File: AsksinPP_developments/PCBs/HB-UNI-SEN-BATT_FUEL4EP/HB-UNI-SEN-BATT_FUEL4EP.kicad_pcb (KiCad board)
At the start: 2 copper layers, 75 x 75 mm, 25 parts, among them J1 Conn_01x02, J10 charge, J2 Conn_01x02, J3 Conn_01x02, J4 Conn_01x02, J5 ISP Programmer, J6 Conn_01x04, J7 Conn_01x04, J8 Conn_01x04, J9 Conn_01x04, Q1 IRLU024N, SW1 config button

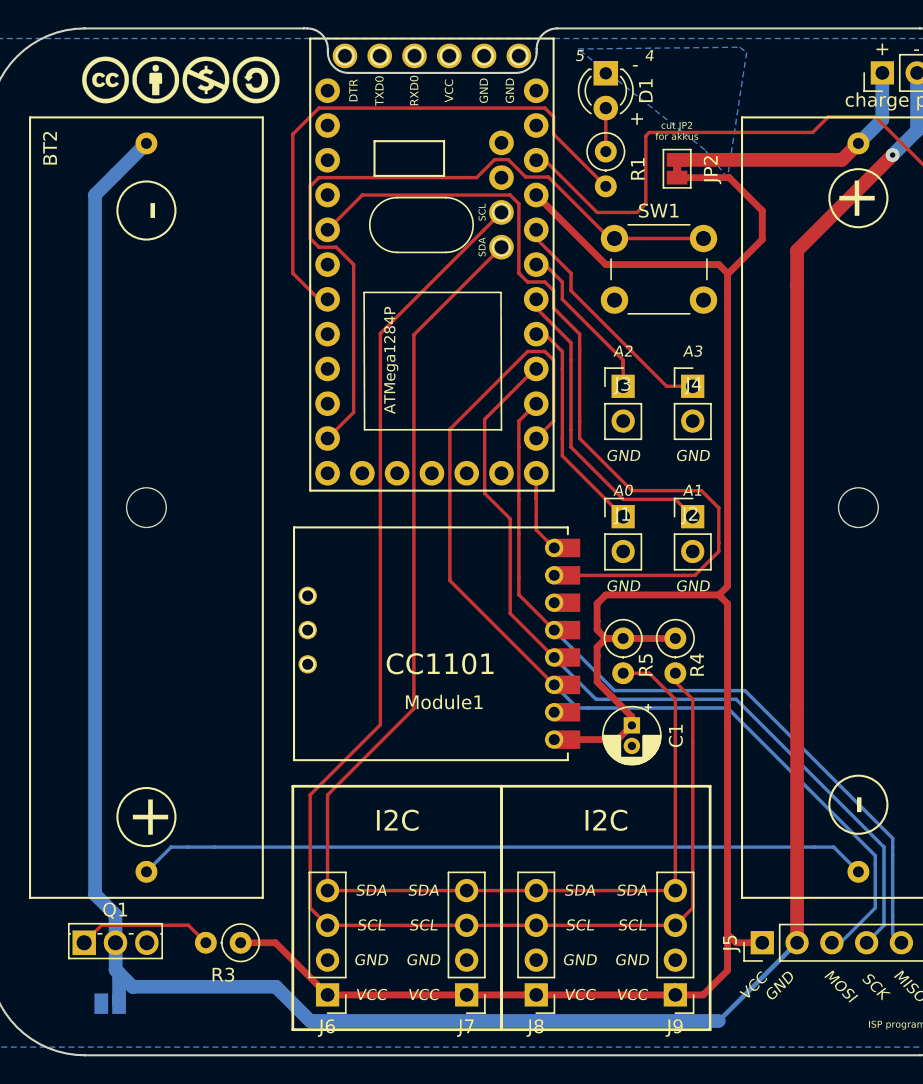
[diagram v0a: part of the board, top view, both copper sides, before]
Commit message: PCBs/HB-UNI-SEN-BATT_FUEL4EP updates, now with gerber data for JLCPCB (not yet vaalidated by prototype!)
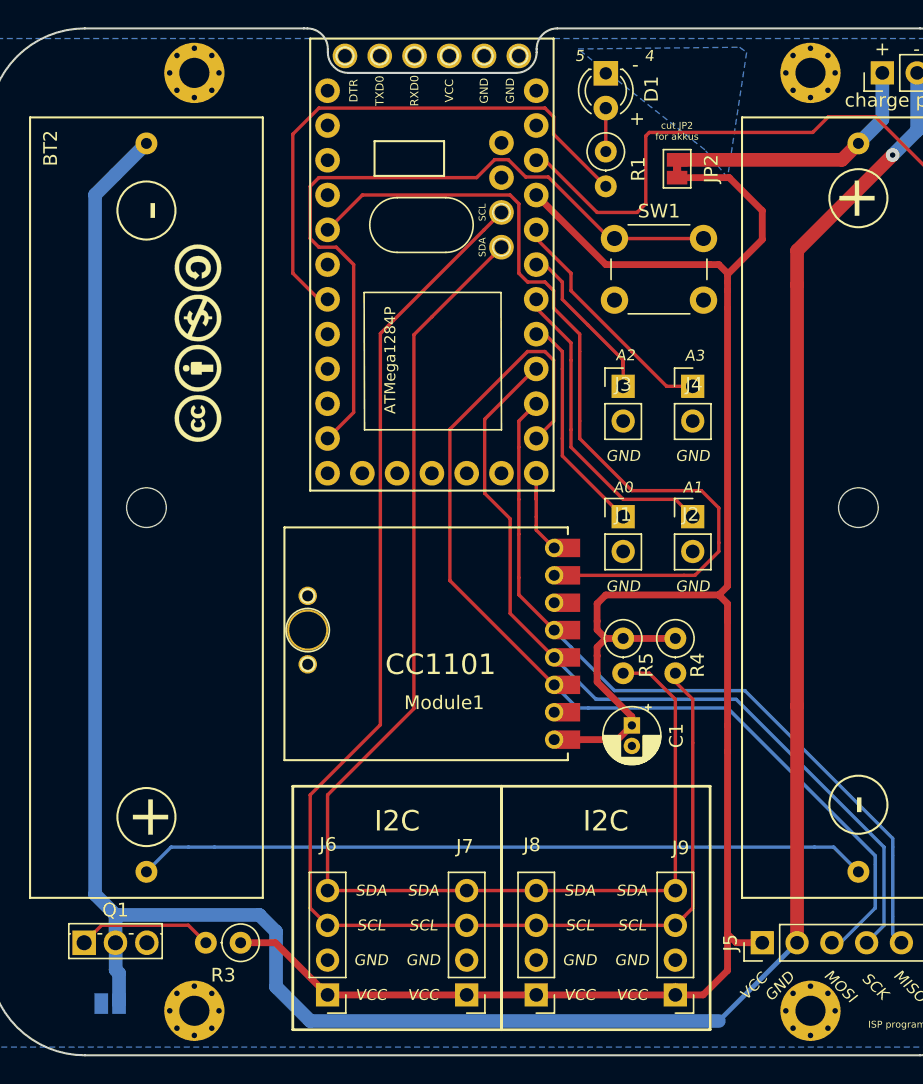
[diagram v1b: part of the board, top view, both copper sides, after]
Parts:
- removed ?: , FUEL4EP:CC-BY-ND-SA
- added H1: MountingHole, FUEL4EP:MountingHole_2.2mm_M2_Pad_Via, F.Cu at (116.0, 81.2)
- added H2: MountingHole, FUEL4EP:MountingHole_2.2mm_M2_Pad_Via, F.Cu at (161.0, 81.2)
- added H3: MountingHole, FUEL4EP:MountingHole_2.2mm_M2_Pad_Via, F.Cu at (116.0, 149.8)
- added H4: MountingHole, FUEL4EP:MountingHole_2.2mm_M2_Pad_Via, F.Cu at (161.0, 149.8)
- added LOGO1: Logo_Open_Hardware_Small, FUEL4EP:CC-BY-ND-SA, F.Cu at (116.2, 101.0)
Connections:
- Module1 pad 1A: Net-(Module1-Pad1A) -> GND
- Module1 pad 3A: Net-(Module1-Pad3A) -> GND
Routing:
- net /minusBAT: track 186.5 -> 190.5 mm

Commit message: Updates of PCBs/HB-UNI-SEN-BATT_FUEL4EP and HB-UNI-SEN-BATT_E07-868MS10_FUEL4EP
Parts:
- BT1, BT2: footprint FUEL4EP:BATTERY_HOLDER_GOOBAY_AA -> FUEL4EP:BatteryHolder_Keystone_2460_1xAA
- moved BT1 55.3 mm to (164.5, 86.9), turned to 270 degrees
- moved BT2 55.0 mm to (112.4, 138.9), turned to 90 degrees
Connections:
- net Net-(BT1-Pad2) renamed /conBAT
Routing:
- net /MOSI: track 75.9 -> 77.1 mm
- net /conBAT: track 53.5 -> 52.7 mm
- net /minusBAT: track 190.5 -> 189.9 mm
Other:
- board text added: "config"
- board text added: "cut JP2 for accus"
- board text removed: "4"
- board text removed: "5"
- board text removed: "cut JP2 for akkus"

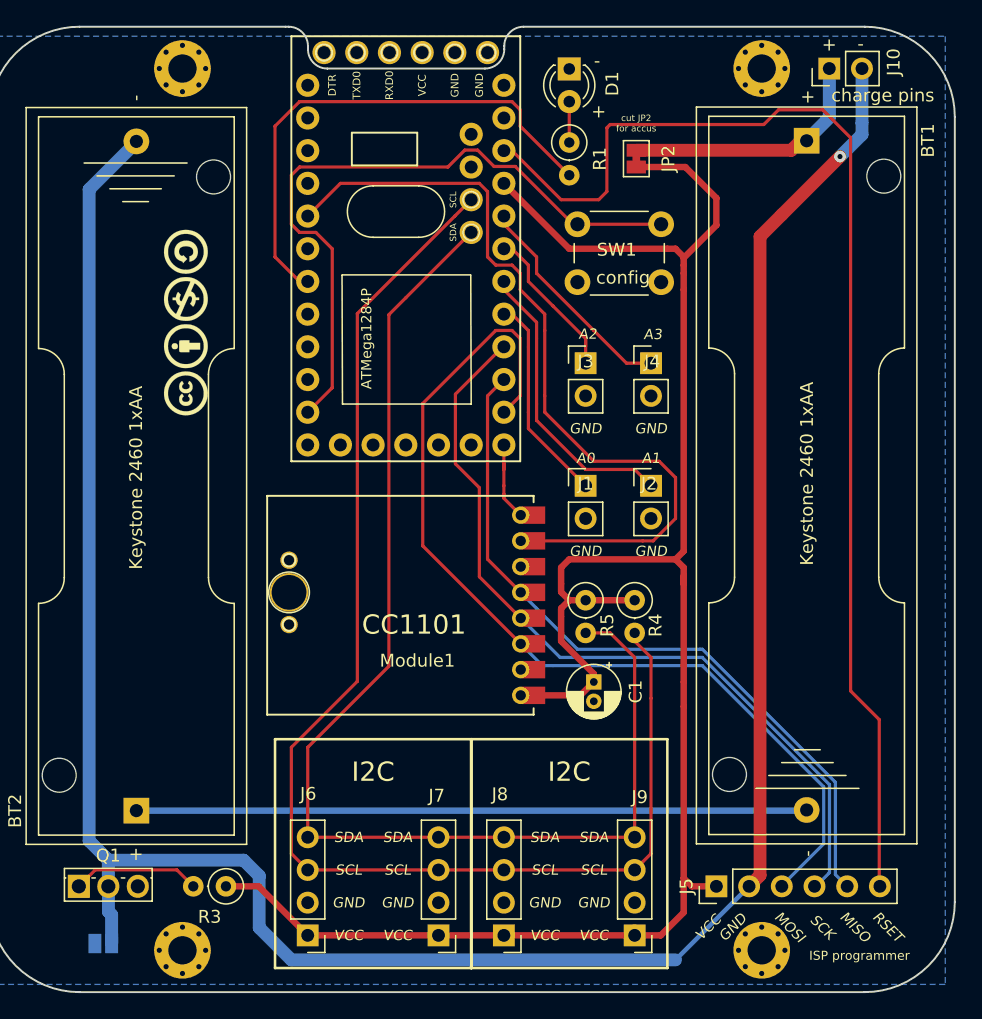
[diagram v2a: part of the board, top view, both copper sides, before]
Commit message: Update of PCBs / added PCBs/HB-UNI-SEN-BATT_ATMega1284P_E07-868MS10_FUEL4EP (all draft only, not yet validated)
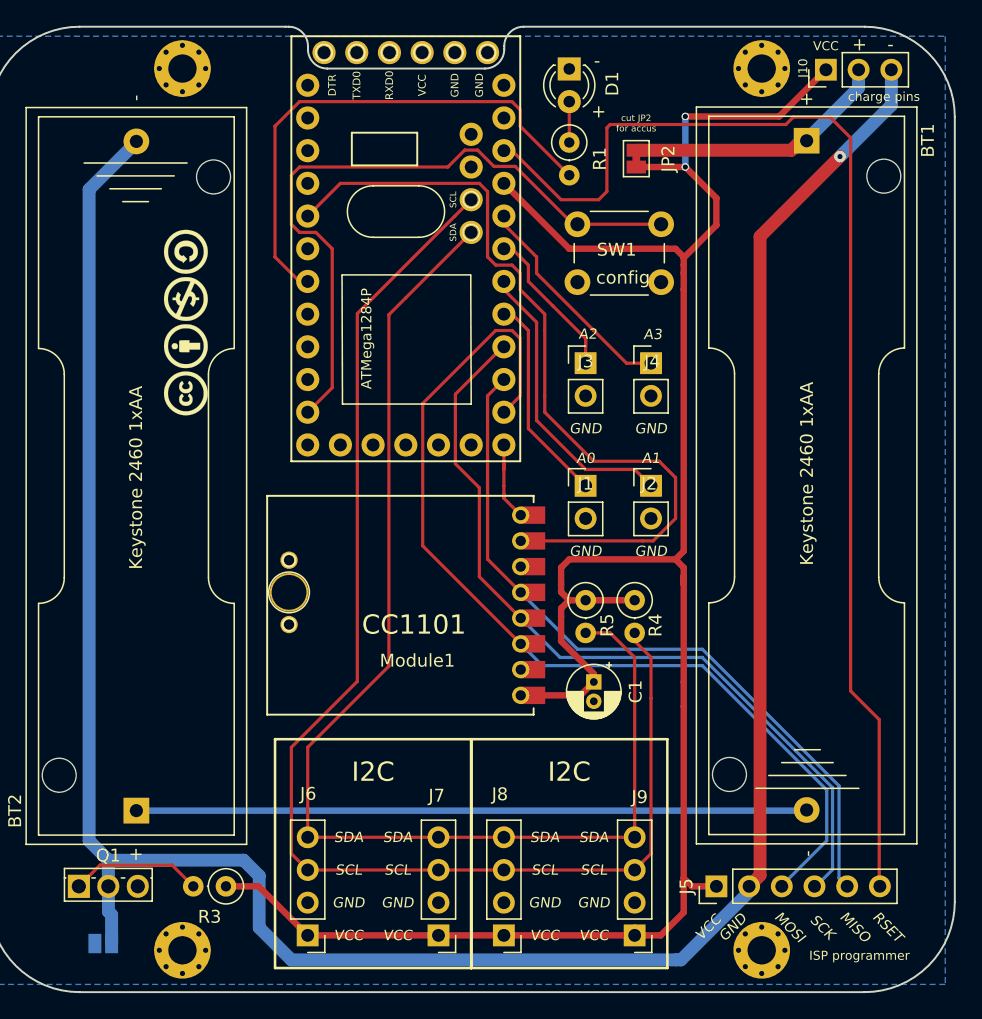
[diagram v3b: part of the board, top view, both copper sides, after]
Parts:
- J10: footprint Connector_PinHeader_2.54mm:PinHeader_1x02_P2.54mm_Vertical -> Connector_PinHeader_2.54mm:PinHeader_1x03_P2.54mm_Vertical
- moved J10 0.28 mm to (166.0, 81.3)
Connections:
- J10 pad 1: /plusBAT -> VCC
- J10 pad 2: /minusBAT -> /plusBAT
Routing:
- net VCC: track 155.1 -> 171.4 mm, vias 0 -> 2
- net /plusBAT: track 19.7 -> 20.8 mm
- net /minusBAT: track 189.9 -> 190.7 mm

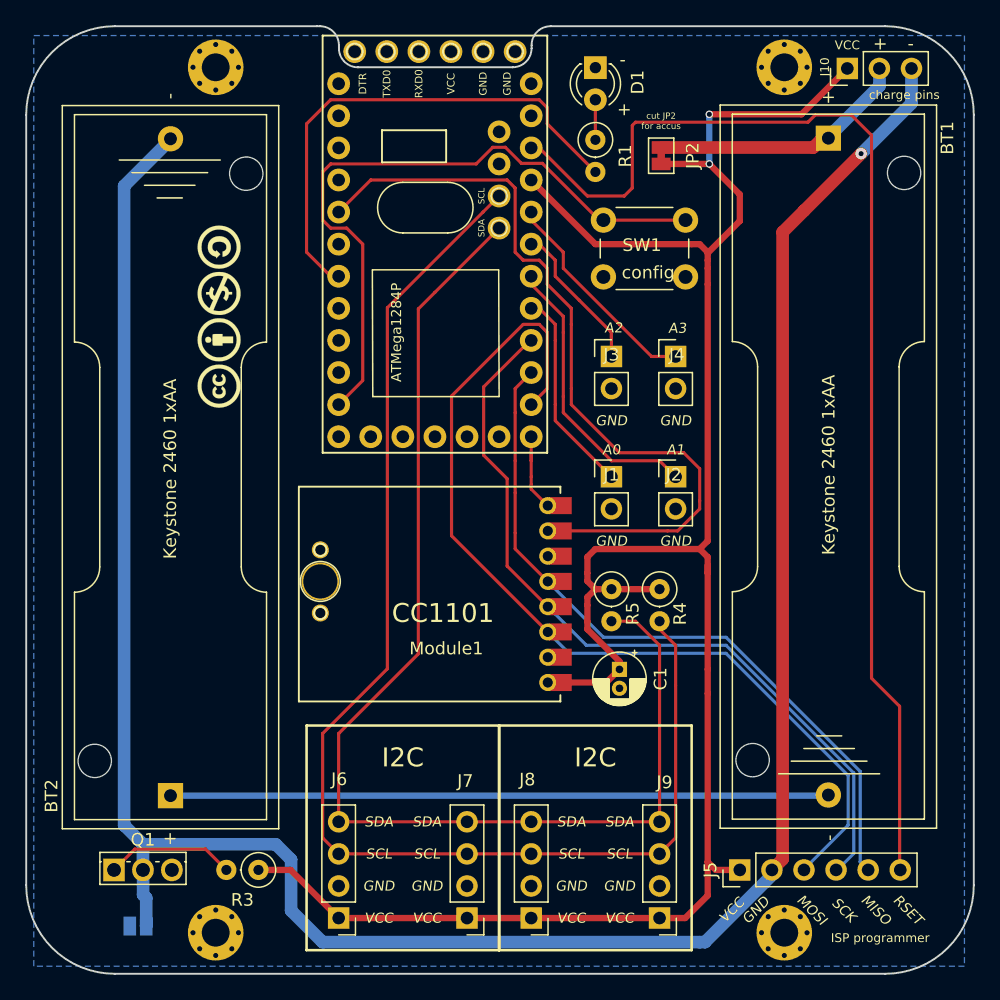
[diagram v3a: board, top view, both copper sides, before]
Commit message: major update: hb-ep-devices-addon V1.14; added sketches HB-UNI-Sensor1-AQ-BME680_KF_rLF and HB-UNI-SenAct-4-4-SC_DS; migration of all PPCBs to KiCAD 6
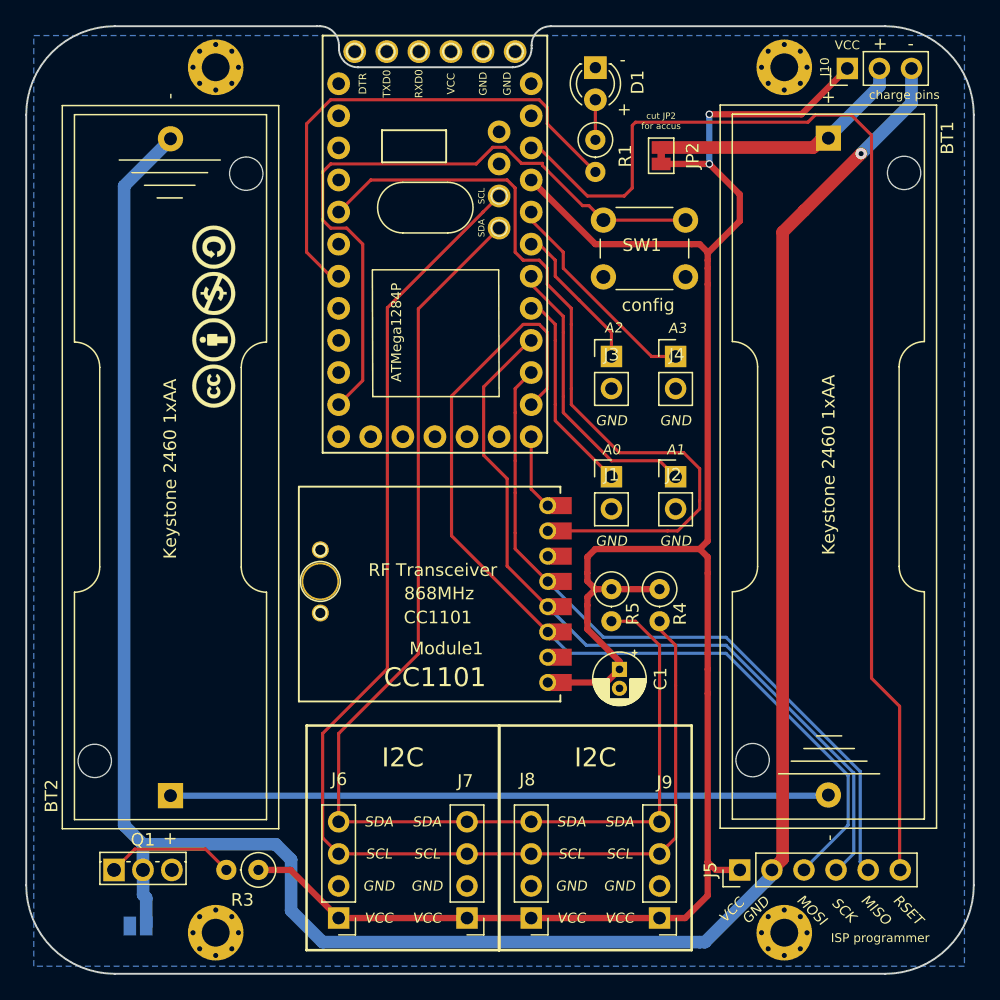
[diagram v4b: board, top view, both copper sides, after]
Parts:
- moved LOGO1 0.43 mm to (115.8, 101.0)
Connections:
- net Net-(Module2-Pad11C) renamed /CONFIG
- Module1 pad 2A: Net-(Module1-Pad2A) -> unconnected-(Module1-Pad2A)
- Module1 pad 6C: Net-(Module1-Pad6C) -> unconnected-(Module1-Pad6C)
- Module2 pad 10C: Net-(Module2-Pad10C) -> unconnected-(Module2-Pad10C)
- Module2 pad 12C: Net-(Module2-Pad12C) -> unconnected-(Module2-Pad12C)
- Module2 pad 1A: Net-(Module2-Pad1A) -> unconnected-(Module2-Pad1A)
- Module2 pad 1B: Net-(Module2-Pad1B) -> unconnected-(Module2-Pad1B)
- Module2 pad 1C: Net-(Module2-Pad1C) -> unconnected-(Module2-Pad1C)
- Module2 pad 1D: Net-(Module2-Pad1D) -> unconnected-(Module2-Pad1D)
- Module2 pad 1E: Net-(Module2-Pad1E) -> unconnected-(Module2-Pad1E)
- Module2 pad 2B: Net-(Module2-Pad2B) -> unconnected-(Module2-Pad2B)
- Module2 pad 2C: Net-(Module2-Pad2C) -> unconnected-(Module2-Pad2C)
- Module2 pad 2D: Net-(Module2-Pad2D) -> unconnected-(Module2-Pad2D)
- Module2 pad 3B: Net-(Module2-Pad3B) -> unconnected-(Module2-Pad3B)
- Module2 pad 3C: Net-(Module2-Pad3C) -> unconnected-(Module2-Pad3C)
- Module2 pad 3D: Net-(Module2-Pad3D) -> unconnected-(Module2-Pad3D)
- Module2 pad 4B: Net-(Module2-Pad4B) -> unconnected-(Module2-Pad4B)
- Module2 pad 4D: Net-(Module2-Pad4D) -> unconnected-(Module2-Pad4D)
- Module2 pad 5B: Net-(Module2-Pad5B) -> unconnected-(Module2-Pad5B)
- Module2 pad 5D: Net-(Module2-Pad5D) -> unconnected-(Module2-Pad5D)
- Module2 pad 6C: Net-(Module2-Pad6C) -> unconnected-(Module2-Pad6C)
- Module2 pad 6D: Net-(Module2-Pad6D) -> unconnected-(Module2-Pad6D)
- Module2 pad 8C: Net-(Module2-Pad8C) -> unconnected-(Module2-Pad8C)
- Module2 pad 9C: Net-(Module2-Pad9C) -> unconnected-(Module2-Pad9C)
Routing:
- net VCC: track 171.4 -> 169.5 mm
- net /SDA: track 97.8 -> 96.2 mm
- net unconnected-(Module1-Pad6C): track 0.00 -> 1.00 mm
- net Net-(Module1-Pad6C): track 1.00 -> 0.00 mm
- net /conBAT: track 52.7 -> 52.1 mm
- net /A2: track 13.2 -> 12.5 mm
- net /SS: track 7.63 -> 7.00 mm
- net /SCK: track 64.3 -> 63.7 mm
- net /MOSI: track 77.3 -> 76.7 mm
- net /RSET: track 94.3 -> 93.8 mm
- net /minusBAT: track 190.7 -> 190.2 mm
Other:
- net class Default removed
- net class battery removed
- net class supply removed
- board text added: "HB-UNI-SENS-BATT_FUEL4EP V1.1"
- board text added: "Version 1.1 - 07/2023 (KiCAD 6)"
- board text removed: "HB-UNI-SENS-BATT_FUEL4EP"
- board text removed: "Version 1.0 - 10/2021"

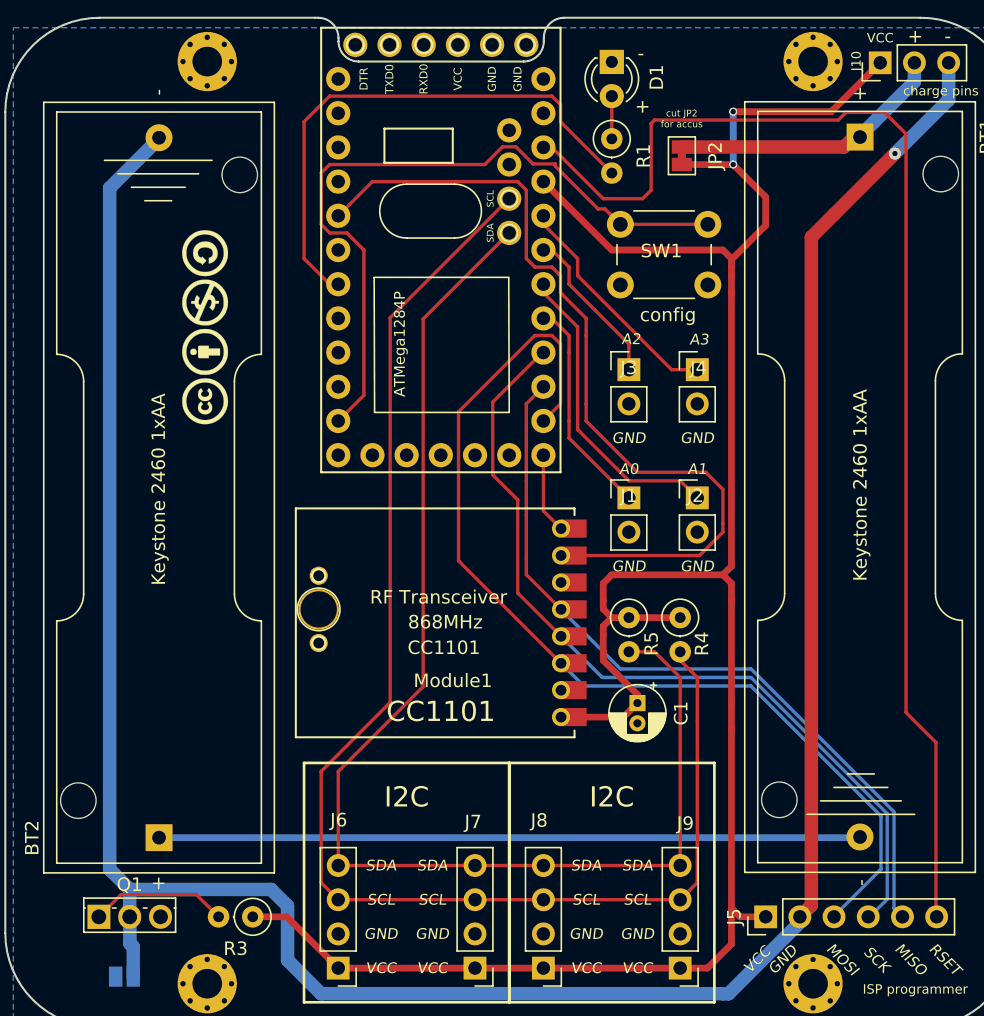
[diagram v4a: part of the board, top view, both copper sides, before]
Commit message: PCBs: KiCAD6 required improvements of layout data bases; added E07-900M10S into FUEL and footprint library
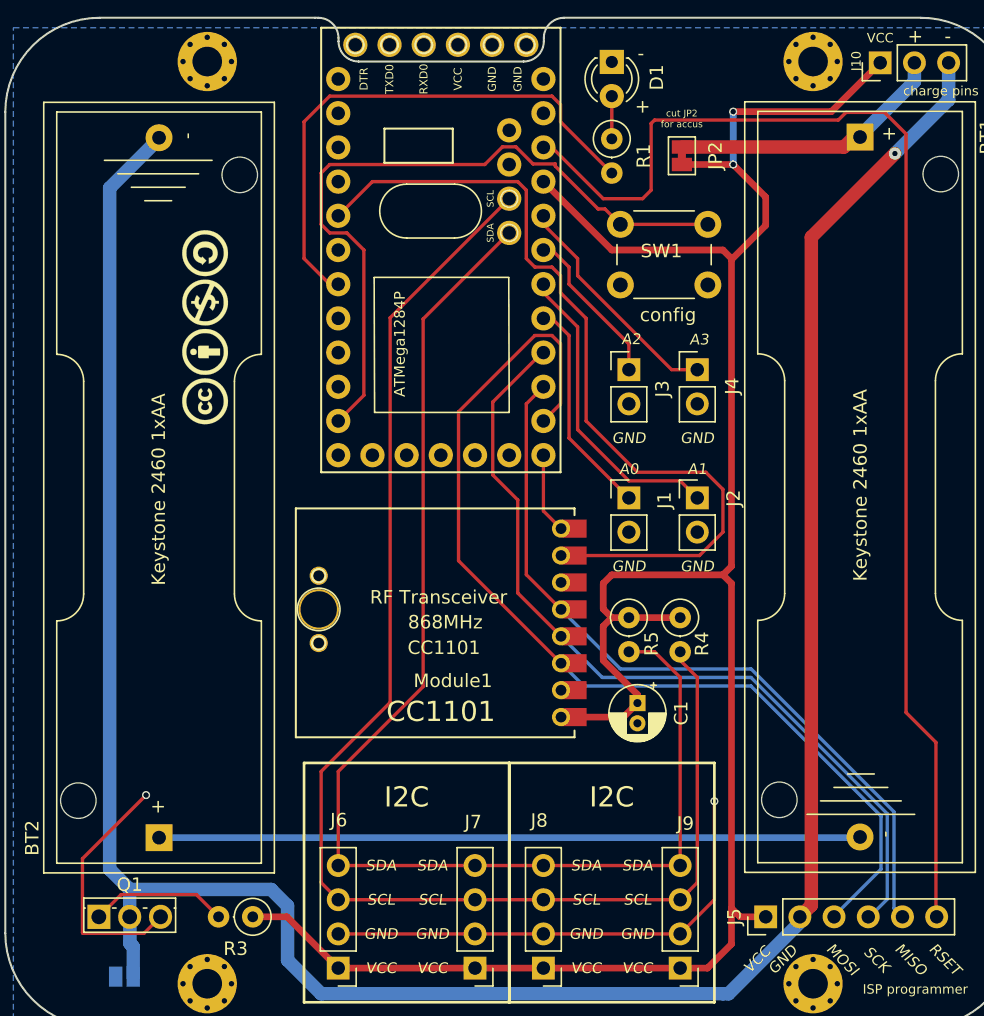
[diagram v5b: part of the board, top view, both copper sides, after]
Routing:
- net GND: track 1.00 -> 55.8 mm, vias 0 -> 2
- net /A2: track 12.5 -> 11.3 mm
- net Net-(Module2-Pad7C): track 40.2 -> 39.6 mm
- net /SCL: track 103.2 -> 102.6 mm
- net /A3: track 17.3 -> 16.6 mm
- net /RSET: track 93.8 -> 93.1 mm
- net /A1: track 22.8 -> 22.2 mm
- net /A0: track 16.3 -> 15.7 mm
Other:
- board text added: "HB-UNI-SENS-BATT_FUEL4EP"
- board text added: "Version 1.2 - 07/2023 (KiCAD 6)"
- board text removed: "HB-UNI-SENS-BATT_FUEL4EP V1.1"
- board text removed: "Version 1.1 - 07/2023 (KiCAD 6)"
